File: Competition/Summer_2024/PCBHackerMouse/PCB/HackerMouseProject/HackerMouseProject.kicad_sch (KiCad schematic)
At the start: 42 parts, among them J1 MicroUSB, SW1 1825910-6, SW3 1825910-6, U1 ESP32-S3R8, U2 W25Q128JVSIM_TR, Y1 ECS-400-10-37B2-CKY-TR

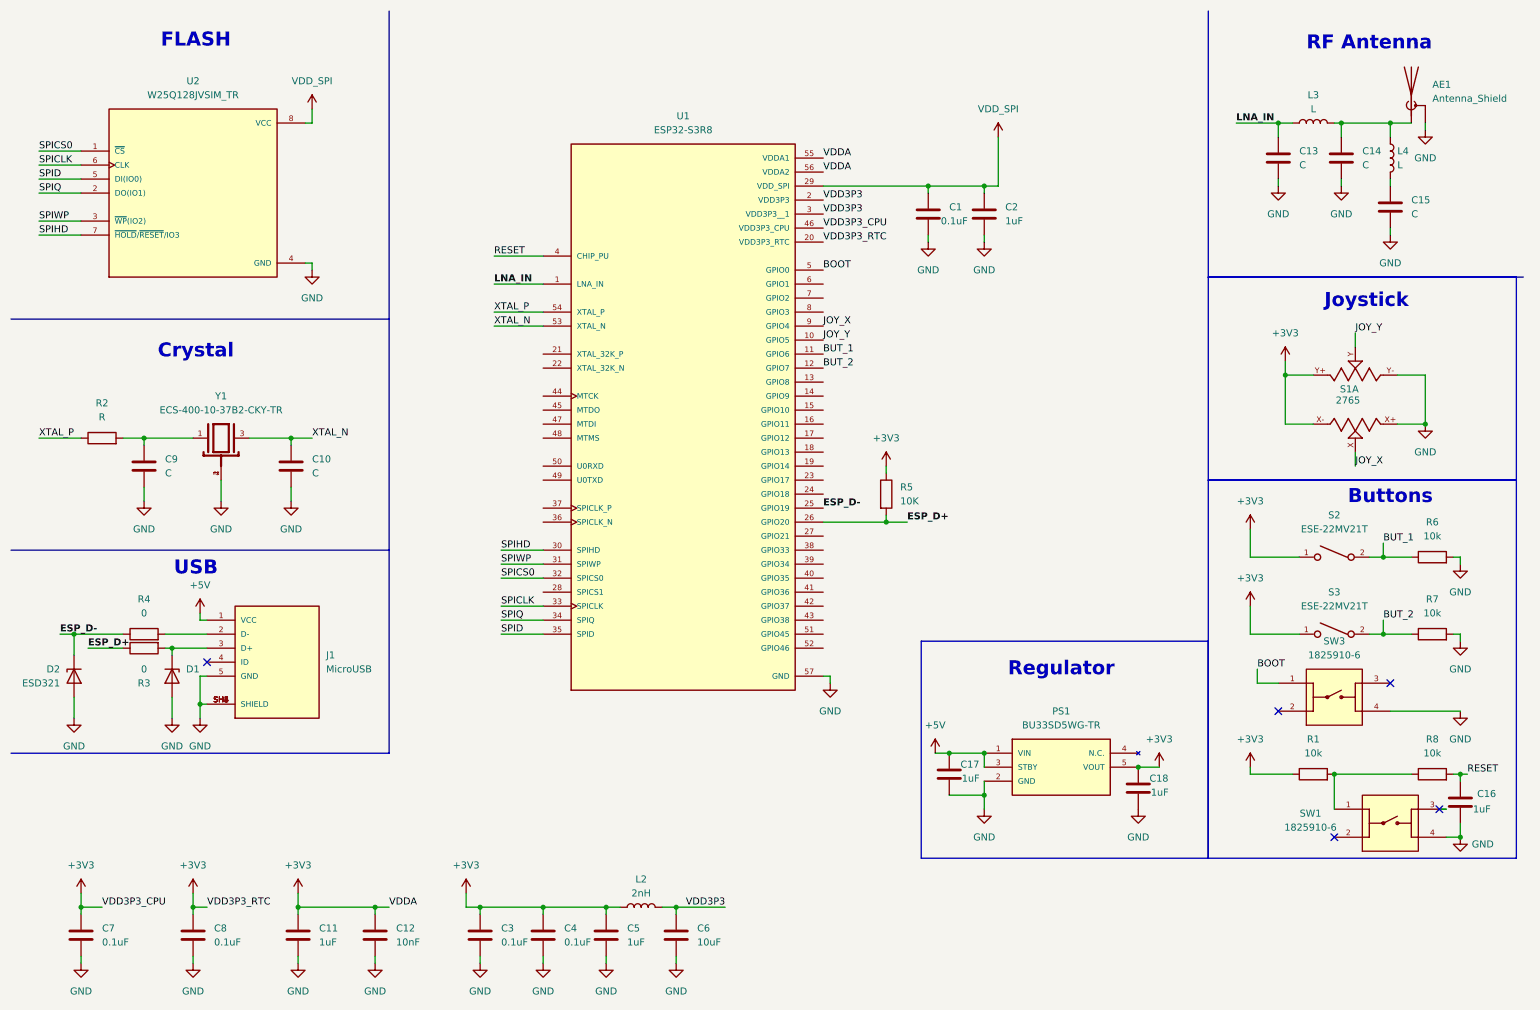
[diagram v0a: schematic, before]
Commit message: Schematic finished
The schematic is finished, but some component value needs to be determined
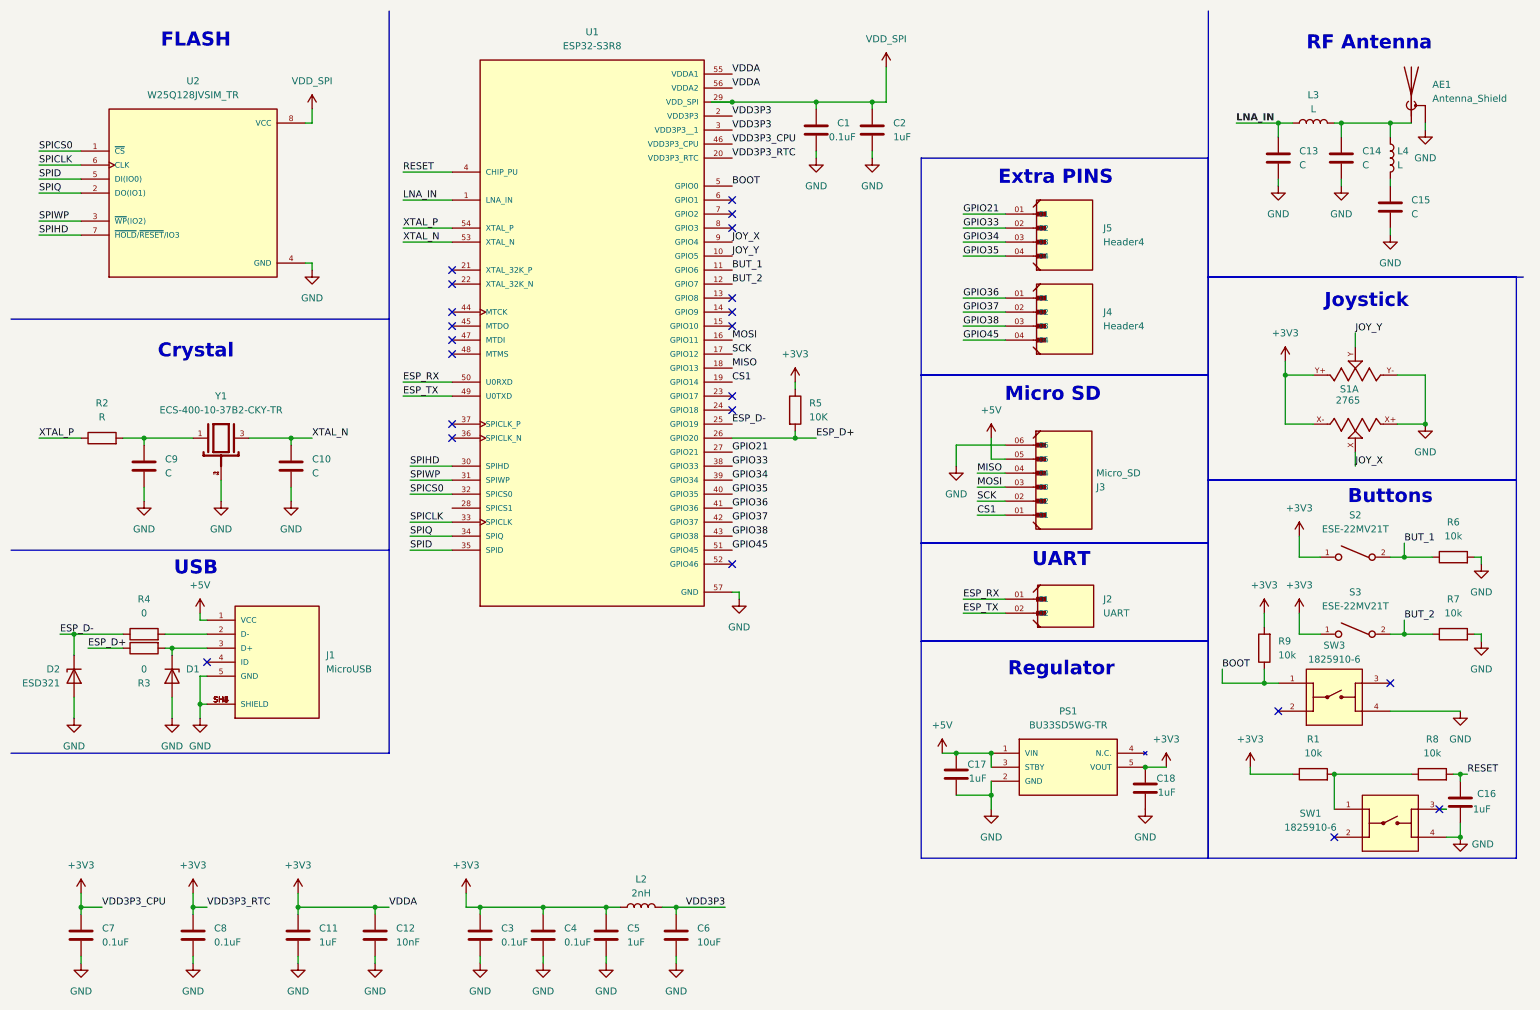
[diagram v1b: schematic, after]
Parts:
- added J2: UART, Header2:WURTH_61300211121, symbol Header2:61300211121
- added J3: Micro_SD, Header6:WURTH_61300611121, symbol Header6:61300611121
- added J4, J5: Header4, Header4:WURTH_61300411121, symbol Header4:61300411121
- added R9: 10k, Resistor_SMD:R_0603_1608Metric_Pad0.98x0.95mm_HandSolder, symbol Device:R
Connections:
- net +3V3: now also R9.2
- net +5V: now also J3.05
- net BOOT: now also R9.1
- net GND: now also J3.06
- net MOSI: now reaches U1.16 (GPIO11)
- net MOSI: now also J3.03
- net SCK: now reaches U1.17 (GPIO12)
- net SCK: now also J3.02
- net MISO: now reaches U1.18 (GPIO13)
- net MISO: now also J3.04
- net CS1: now reaches U1.19 (GPIO14)
- net CS1: now also J3.01
- net GPIO21: now reaches U1.27 (GPIO21)
- net GPIO21: now also J5.01
- net GPIO33: now reaches U1.38 (GPIO33)
- net GPIO33: now also J5.02
- net GPIO34: now reaches U1.39 (GPIO34)
- net GPIO34: now also J5.03
- net GPIO35: now reaches U1.40 (GPIO35)
- net GPIO35: now also J5.04
- net GPIO36: now reaches U1.41 (GPIO36)
- net GPIO36: now also J4.01
- net GPIO37: now reaches U1.42 (GPIO37)
- net GPIO37: now also J4.02
- net GPIO38: now reaches U1.43 (GPIO38)
- net GPIO38: now also J4.03
- net ESP_TX: now reaches U1.49 (U0TXD)
- net ESP_TX: now also J2.02
- net ESP_RX: now reaches U1.50 (U0RXD)
- net ESP_RX: now also J2.01
- net GPIO45: now reaches U1.51 (GPIO45)
- net GPIO45: now also J4.04
- no-connect marks 5 -> 22
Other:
- note added: "Extra PINS"
- note added: "Micro SD"
- note added: "UART"
- moved on the sheet: C1, C17, C18, C2, PS1, R5, R6, R7, S2, S3, U1

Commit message: First placement of component
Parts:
- added J6: POWER, Header2:WURTH_61300211121, symbol Header2:61300211121
- C10, C9: value C -> 12pF
- C13, C14: value C -> 1pF
- L2: value 2nH -> 2.4nH; footprint (none) -> Capacitor_SMD:C_0603_1608Metric_Pad1.08x0.95mm_HandSolder
- L3: value L -> 2.4 nH; footprint (none) -> Capacitor_SMD:C_0603_1608Metric_Pad1.08x0.95mm_HandSolder
- L4: footprint (none) -> Capacitor_SMD:C_0603_1608Metric_Pad1.08x0.95mm_HandSolder
- R2: value R -> 22
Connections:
- net +5V: now also J6.01
- net ESP_D-: no longer D2.1 (K)
- net GND: now also J6.02
- net at J1.2 (D-), R4.2: now also D2.1 (K)
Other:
- note added: "POWER"
- moved on the sheet: R4

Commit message: Start Tracing PCB
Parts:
- added R10: 10k, Resistor_SMD:R_0603_1608Metric_Pad0.98x0.95mm_HandSolder, symbol Device:R
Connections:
- net +5V: now also R10.2; no longer PS1.3 (STBY)
- new net: PS1.3 (STBY), R10.1
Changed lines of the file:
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@@
 	)
 	(junction
-		(at 189.23 146.05)
-		(diameter 0)
-		(color 0 0 0 0)
-	)
-	(junction
 		(at 157.48 27.94)
 		(diameter 0)
@@
 	(wire
 		(pts
+			(xy 187.96 148.59) (xy 189.23 148.59)
+		)
+		(stroke
+			(width 0)
+			(type default)
+		)
+	)
+	(wire
+		(pts
 			(xy 107.95 182.88) (xy 107.95 184.15)
 		)
@@
 	(wire
 		(pts
+			(xy 187.96 135.89) (xy 187.96 137.16)
+		)
+		(stroke
+			(width 0)
+			(type default)
+		)
+	)
+	(wire
+		(pts
 			(xy 82.55 40.64) (xy 91.44 40.64)
 		)
@@
 	(wire
 		(pts
-			(xy 182.88 146.05) (xy 180.34 146.05)
-		)
-		(stroke
-			(width 0)
-			(type default)
-		)
-	)
-	(wire
-		(pts
 			(xy 82.55 53.34) (xy 91.44 53.34)
 		)
@@
 	(wire
 		(pts
+			(xy 180.34 146.05) (xy 182.88 146.05)
+		)
+		(stroke
+			(width 0)
+			(type default)
+		)
+	)
+	(wire
+		(pts
 			(xy 184.15 50.8) (xy 191.77 50.8)
 		)
@@
 	(wire
 		(pts
-			(xy 189.23 146.05) (xy 189.23 148.59)
-		)
-		(stroke
-			(width 0)
-			(type default)
-		)
-	)
-	(wire
-		(pts
 			(xy 167.64 36.83) (xy 167.64 38.1)
 		)
@@
 	(wire
 		(pts
+			(xy 187.96 144.78) (xy 187.96 148.59)
+		)
+		(stroke
+			(width 0)
+			(type default)
+		)
+	)
+	(wire
+		(pts
 			(xy 191.77 90.17) (xy 182.88 90.17)
 		)
@@
 	(wire
 		(pts
+			(xy 180.34 135.89) (xy 180.34 146.05)
+		)
+		(stroke
+			(width 0)
+			(type default)
+		)
+	)
+	(wire
+		(pts
 			(xy 276.86 110.49) (xy 278.13 110.49)
 		)
@@
 	(symbol
 		(lib_id "Device:R")
+		(at 187.96 140.97 180)
+		(unit 1)
+		(exclude_from_sim no)
+		(in_bom yes)
+		(on_board yes)
+		(dnp no)
+		(fields_autoplaced yes)
+		(property "Reference" "R10"
+			(at 190.5 139.6999 0)
+			(effects
+				(font
+					(size 1.27 1.27)
+				)
+				(justify right)
+			)
+		)
+		(property "Value" "10k"
+			(at 190.5 142.2399 0)
+			(effects
+				(font
+					(size 1.27 1.27)
+				)
+				(justify right)
+			)
+		)
+		(property "Footprint" "Resistor_SMD:R_0603_1608Metric_Pad0.98x0.95mm_HandSolder"
+			(at 189.738 140.97 90)
+			(effects
+				(font
+					(size 1.27 1.27)
+				)
+				(hide yes)
+			)
+		)
+		(property "Datasheet" "~"
+			(at 187.96 140.97 0)
+			(effects
+				(font
+					(size 1.27 1.27)
+				)
+				(hide yes)
+			)
+		)
+		(property "Description" "Resistor"
+			(at 187.96 140.97 0)
+			(effects
+				(font
+					(size 1.27 1.27)
+				)
+				(hide yes)
+			)
+		)
+		(pin "2"
+		)
+		(pin "1"
+		)
+		(instances
+			(project "HackerMouseProject"
+				(path "/97558d47-9d67-4b31-b5fa-18b7f4cf0498"
+					(reference "R10")
+					(unit 1)
+				)
+			)
+		)
+	)
+	(symbol
+		(lib_id "Device:R")
 		(at 27.94 88.9 90)
 		(unit 1)
@@
 	)
 	(symbol
+		(lib_id "power:+5V")
+		(at 187.96 135.89 0)
+		(unit 1)
+		(exclude_from_sim no)
+		(in_bom yes)
+		(on_board yes)
+		(dnp no)
+		(fields_autoplaced yes)
+		(property "Reference" "#PWR049"
+			(at 187.96 139.7 0)
+			(effects
+				(font
+					(size 1.27 1.27)
+				)
+				(hide yes)
+			)
+		)
+		(property "Value" "+5V"
+			(at 187.96 130.81 0)
+			(effects
+				(font
+					(size 1.27 1.27)
+				)
+			)
+		)
+		(property "Footprint" ""
+			(at 187.96 135.89 0)
+			(effects
+				(font
+					(size 1.27 1.27)
+				)
+				(hide yes)
+			)
+		)
+		(property "Datasheet" ""
+			(at 187.96 135.89 0)
+			(effects
+				(font
+					(size 1.27 1.27)
+				)
+				(hide yes)
+			)
+		)
+		(property "Description" "Power symbol creates a global label with name \"+5V\""
+			(at 187.96 135.89 0)
+			(effects
+				(font
+					(size 1.27 1.27)
+				)
+				(hide yes)
+			)
+		)
+		(pin "1"
+		)
+		(instances
+			(project "HackerMouseProject"
+				(path "/97558d47-9d67-4b31-b5fa-18b7f4cf0498"
+					(reference "#PWR049")
+					(unit 1)
+				)
+			)
+		)
+	)
+	(symbol
 		(lib_id "power:GND")
 		(at 241.3 43.18 0)
@@
 	(symbol
 		(lib_id "power:+5V")
-		(at 180.34 146.05 0)
+		(at 180.34 135.89 0)
 		(unit 1)
 		(exclude_from_sim no)
@@
 		(fields_autoplaced yes)
 		(property "Reference" "#PWR042"
-			(at 180.34 149.86 0)
+			(at 180.34 139.7 0)
 			(effects
 				(font
@@
 		)
 		(property "Value" "+5V"
-			(at 180.34 140.97 0)
+			(at 180.34 130.81 0)
 			(effects
 				(font
@@
 		)
 		(property "Footprint" ""
-			(at 180.34 146.05 0)
+			(at 180.34 135.89 0)
 			(effects
 				(font
@@
 		)
 		(property "Datasheet" ""
-			(at 180.34 146.05 0)
+			(at 180.34 135.89 0)
 			(effects
 				(font
@@
 		)
 		(property "Description" "Power symbol creates a global label with name \"+5V\""
-			(at 180.34 146.05 0)
+			(at 180.34 135.89 0)
 			(effects
 				(font
@@
 		(dnp no)
 		(property "Reference" "C17"
-			(at 184.912 148.082 0)
+			(at 176.784 149.86 0)
 			(effects
 				(font
@@
 		)
 		(property "Value" "1uF"
-			(at 185.166 150.622 0)
+			(at 177.038 152.4 0)
 			(effects
 				(font
